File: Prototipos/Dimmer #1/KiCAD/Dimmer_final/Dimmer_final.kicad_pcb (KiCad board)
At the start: 2 copper layers, 50 x 100 mm, 32 parts, among them J2 Conn_01x02, K1 SRD-05VDC-SL-C, M5_BotL MountingHole_5.3mm_M5, M5_BotR MountingHole_5.3mm_M5, M5_TopL MountingHole_5.3mm_M5, M5_TopR MountingHole_5.3mm_M5, Q1 BC548B, Q2 BT137, U1 MOC3021M, U2 EL817

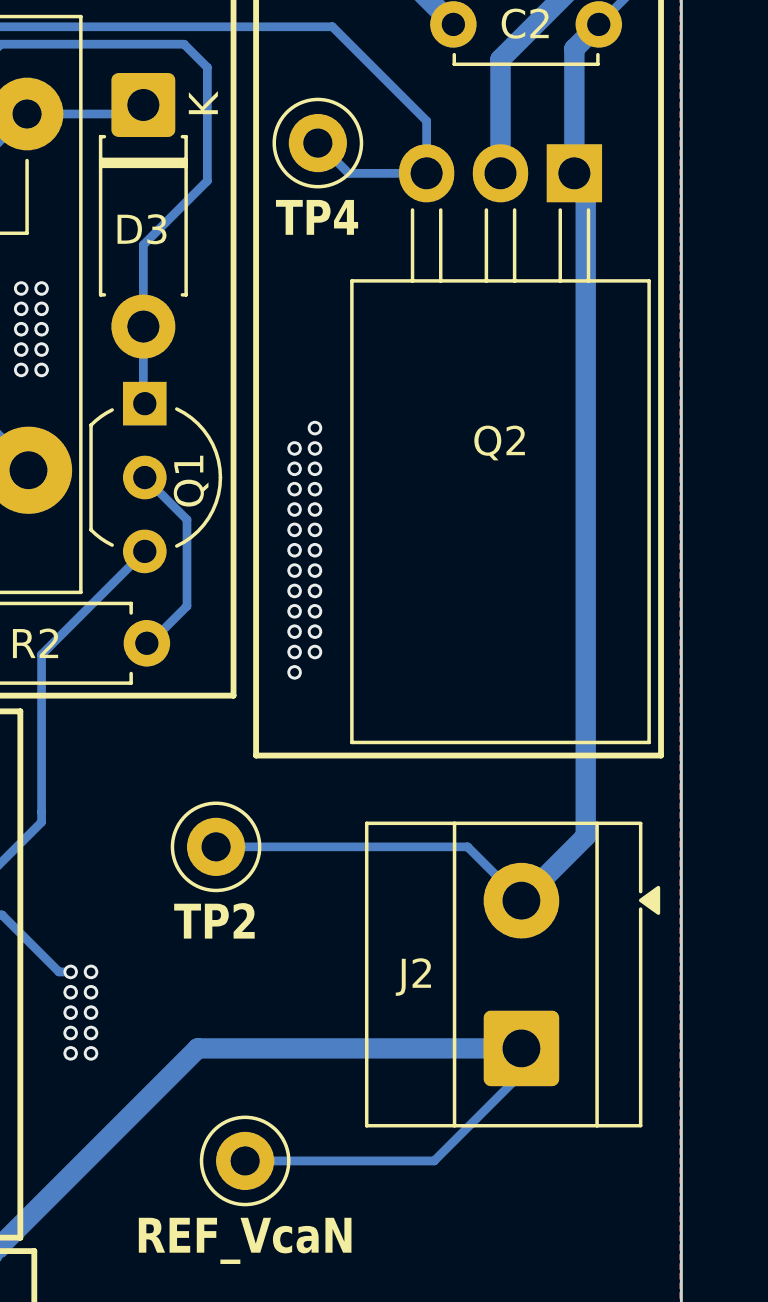
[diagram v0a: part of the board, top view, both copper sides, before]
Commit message: Actualizar footprints
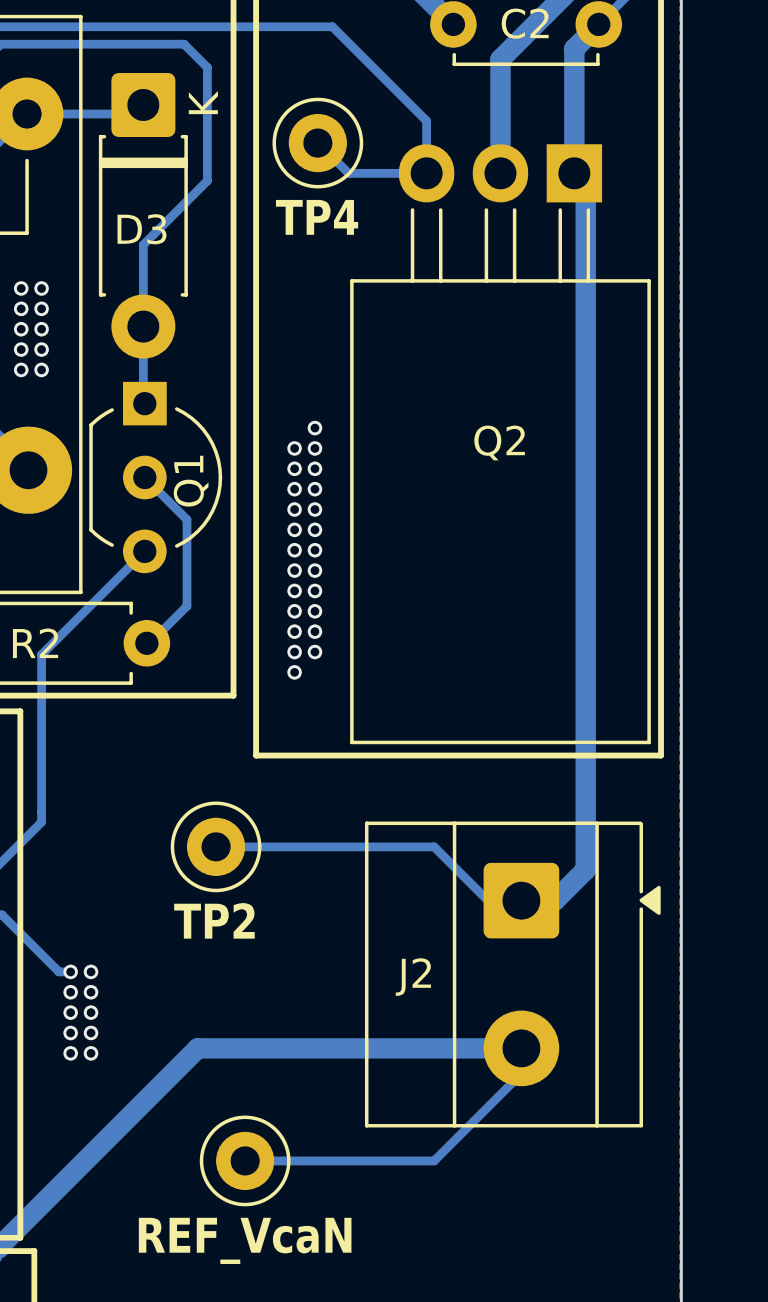
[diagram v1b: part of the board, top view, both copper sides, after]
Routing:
- net LOAD_L: track 87.8 -> 88.4 mm
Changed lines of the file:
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@@
 		)
 		(embedded_fonts no)
-		(model "${KIPRJMOD}/../../../../KiCad-Libraries/RV09AF-40-20K-B10K--3DModel-STEP-510211.STEP"
+		(model "${KICAD9_3DMODEL_DIR}/Potentiometer_THT.3dshapes/Potentiometer_Alps_RK09K_Single_Vertical.step"
 			(offset
-				(xyz 7 -2.5 0)
+				(xyz 0 0 0)
 			)
 			(scale
@@
 			)
 			(rotate
-				(xyz -90 -0 90)
+				(xyz 0 0 0)
 			)
 		)
@@
 		)
 		(embedded_fonts no)
-		(model "${KIPRJMOD}/../../../../KiCad-Libraries/MOC3021.step"
-			(offset
-				(xyz 0 0 0)
-			)
-			(scale
-				(xyz 1 0.8 1.05)
-			)
-			(rotate
-				(xyz -90 -0 -0)
-			)
-		)
 	)
 	(footprint "TestPoint:TestPoint_Loop_D1.80mm_Drill1.0mm_Beaded"
@@
 		)
 		(fp_line
-			(start 5.39 4.1)
-			(end 7.726447 4.1)
+			(start 5.39 4.12)
+			(end 7.7 4.12)
 			(stroke
 				(width 0.12)
@@
 		)
 		(fp_line
-			(start -2.65 4.1)
-			(end 4.79 4.1)
+			(start -2.65 4.12)
+			(end 4.79 4.12)
 			(stroke
 				(width 0.12)
@@
 		)
 		(fp_line
-			(start -2.66 4.1)
+			(start -2.66 4.12)
 			(end -2.66 -5.32)
 			(stroke
@@
 		(fp_poly
 			(pts
-				(xy 5.09 4.1) (xy 4.65 4.71) (xy 5.53 4.71)
+				(xy 5.09 4.12) (xy 4.65 4.73) (xy 5.53 4.73)
 			)
 			(stroke
@@
 		(fp_line
 			(start 7.62 -5.2)
-			(end 7.62 4.6)
+			(end 7.62 4.1)
 			(stroke
 				(width 0.1)
@@
 		)
 		(fp_line
-			(start -2.54 4.1)
-			(end -2.54 -5.2)
+			(start 7.13 4)
+			(end 7.63 3.5)
 			(stroke
 				(width 0.1)
@@
 		)
 		(fp_line
-			(start -2.54 4.1)
-			(end 7.62 4.1)
+			(start -2.53 4)
+			(end 7.13 4)
 			(stroke
 				(width 0.1)
@@
 		)
 		(fp_line
-			(start 7.62 4.6)
-			(end -2.04 4.6)
+			(start -2.54 4.1)
+			(end -2.54 -5.2)
 			(stroke
 				(width 0.1)
@@
 		)
 		(fp_line
-			(start -2.04 4.6)
-			(end -2.54 4.1)
+			(start -2.54 4.1)
+			(end 7.62 4.1)
 			(stroke
 				(width 0.1)
@@
 			)
 		)
-		(pad "1" thru_hole roundrect
+		(pad "1" thru_hole circle
 			(at 0 0 90)
 			(size 2.6 2.6)
@@
 			(layers "*.Cu" "*.Mask")
 			(remove_unused_layers no)
-			(roundrect_rratio 0.096154)
 			(net 5 "48Vca_N")
 			(pinfunction "Pin_1")
 			(pintype "passive")
 		)
-		(pad "2" thru_hole circle
+		(pad "2" thru_hole roundrect
 			(at 5.08 0 90)
 			(size 2.6 2.6)
@@
 			(layers "*.Cu" "*.Mask")
 			(remove_unused_layers no)
+			(roundrect_rratio 0.09615384615)
 			(net 2 "LOAD_L")
 			(pinfunction "Pin_2")
@@
 		(tags "PCIe")
 		(property "Reference" "J4"
-			(at 11.32 -6.52 180)
+			(at 11.32 -6.52 0)
 			(layer "F.SilkS")
 			(effects
@@
 		)
 		(fp_text user "${REFERENCE}"
-			(at 11.52 -6.53 180)
+			(at 11.52 -6.53 0)
 			(layer "F.Fab")
 			(effects
@@
 	)
 	(segment
-		(start 110.32 57.45)
-		(end 109.69 57.45)
-		(width 0.3)
+		(start 137.65 102.55)
+		(end 138.71 101.49)
+		(width 0.7)
 		(layer "B.Cu")
 		(net 2)
 	)
 	(segment
-		(start 136.5 102.55)
-		(end 134.65 100.7)
+		(start 110.32 57.45)
+		(end 109.69 57.45)
 		(width 0.3)
 		(layer "B.Cu")
@@
 	)
 	(segment
-		(start 138.71 100.34)
+		(start 135.35 102.55)
+		(end 133.5 100.7)
+		(width 0.3)
+		(layer "B.Cu")
+		(net 2)
+	)
+	(segment
+		(start 136.5 102.55)
+		(end 135.35 102.55)
+		(width 0.3)
+		(layer "B.Cu")
+		(net 2)
+	)
+	(segment
+		(start 138.71 101.49)
 		(end 138.71 77.93)
 		(width 0.7)
@@
 	(segment
 		(start 136.5 102.55)
-		(end 138.71 100.34)
+		(end 137.65 102.55)
 		(width 0.7)
 		(layer "B.Cu")
@@
 	)
 	(segment
-		(start 134.65 100.7)
+		(start 133.5 100.7)
 		(end 126 100.7)
 		(width 0.3)

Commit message: Correcciones varias
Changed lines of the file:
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@@
 	)
 	(via
-		(at 114.9 50)
+		(at 114.9 47.9)
 		(size 0.5)
 		(drill 0.3)
@@
 	)
 	(via
-		(at 117 49.3)
+		(at 117 47.2)
 		(size 0.5)
 		(drill 0.3)
@@
 	)
 	(via
-		(at 119.8 49.3)
+		(at 119.8 47.2)
 		(size 0.5)
 		(drill 0.3)
@@
 	)
 	(via
-		(at 120.5 50)
+		(at 120.5 47.9)
 		(size 0.5)
 		(drill 0.3)
@@
 	)
 	(via
-		(at 116.3 50)
+		(at 116.3 47.9)
 		(size 0.5)
 		(drill 0.3)
@@
 	)
 	(via
-		(at 121.2 50)
-		(size 0.5)
-		(drill 0.3)
-		(layers "F.Cu" "B.Cu")
-		(net 11)
-	)
-	(via
-		(at 119.1 49.3)
+		(at 121.2 47.9)
+		(size 0.5)
+		(drill 0.3)
+		(layers "F.Cu" "B.Cu")
+		(net 11)
+	)
+	(via
+		(at 119.1 47.2)
 		(size 0.5)
 		(drill 0.3)
@@
 	)
 	(via
-		(at 113.5 50)
+		(at 113.5 47.9)
 		(size 0.5)
 		(drill 0.3)
@@
 	)
 	(via
-		(at 112.8 49.3)
+		(at 112.8 47.2)
 		(size 0.5)
 		(drill 0.3)
@@
 	)
 	(via
-		(at 120.5 49.3)
+		(at 120.5 47.2)
 		(size 0.5)
 		(drill 0.3)
@@
 	)
 	(via
-		(at 115.6 49.3)
-		(size 0.5)
-		(drill 0.3)
-		(layers "F.Cu" "B.Cu")
-		(net 11)
-	)
-	(via
-		(at 117 50)
+		(at 115.6 47.2)
+		(size 0.5)
+		(drill 0.3)
+		(layers "F.Cu" "B.Cu")
+		(net 11)
+	)
+	(via
+		(at 117 47.9)
 		(size 0.5)
 		(drill 0.3)
@@
 	)
 	(via
-		(at 117.7 49.3)
-		(size 0.5)
-		(drill 0.3)
-		(layers "F.Cu" "B.Cu")
-		(net 11)
-	)
-	(via
-		(at 114.2 50)
+		(at 117.7 47.2)
+		(size 0.5)
+		(drill 0.3)
+		(layers "F.Cu" "B.Cu")
+		(net 11)
+	)
+	(via
+		(at 114.2 47.9)
 		(size 0.5)
 		(drill 0.3)
@@
 	)
 	(via
-		(at 114.2 49.3)
+		(at 114.2 47.2)
 		(size 0.5)
 		(drill 0.3)
@@
 	)
 	(via
-		(at 118.4 49.3)
+		(at 118.4 47.2)
 		(size 0.5)
 		(drill 0.3)
@@
 	)
 	(via
-		(at 115.6 50)
+		(at 115.6 47.9)
 		(size 0.5)
 		(drill 0.3)
@@
 	)
 	(via
-		(at 113.5 49.3)
+		(at 113.5 47.2)
 		(size 0.5)
 		(drill 0.3)
@@
 	)
 	(via
-		(at 117.7 50)
+		(at 117.7 47.9)
 		(size 0.5)
 		(drill 0.3)
@@
 	)
 	(via
-		(at 114.9 49.3)
+		(at 114.9 47.2)
 		(size 0.5)
 		(drill 0.3)
@@
 	)
 	(via
-		(at 119.8 50)
+		(at 119.8 47.9)
 		(size 0.5)
 		(drill 0.3)
@@
 	)
 	(via
-		(at 118.4 50)
+		(at 118.4 47.9)
 		(size 0.5)
 		(drill 0.3)
@@
 	)
 	(via
-		(at 119.1 50)
+		(at 119.1 47.9)
 		(size 0.5)
 		(drill 0.3)
@@
 	)
 	(via
-		(at 116.3 49.3)
-		(size 0.5)
-		(drill 0.3)
+		(at 116.3 47.2)
+		(size 0.5)
+		(drill 0.3)

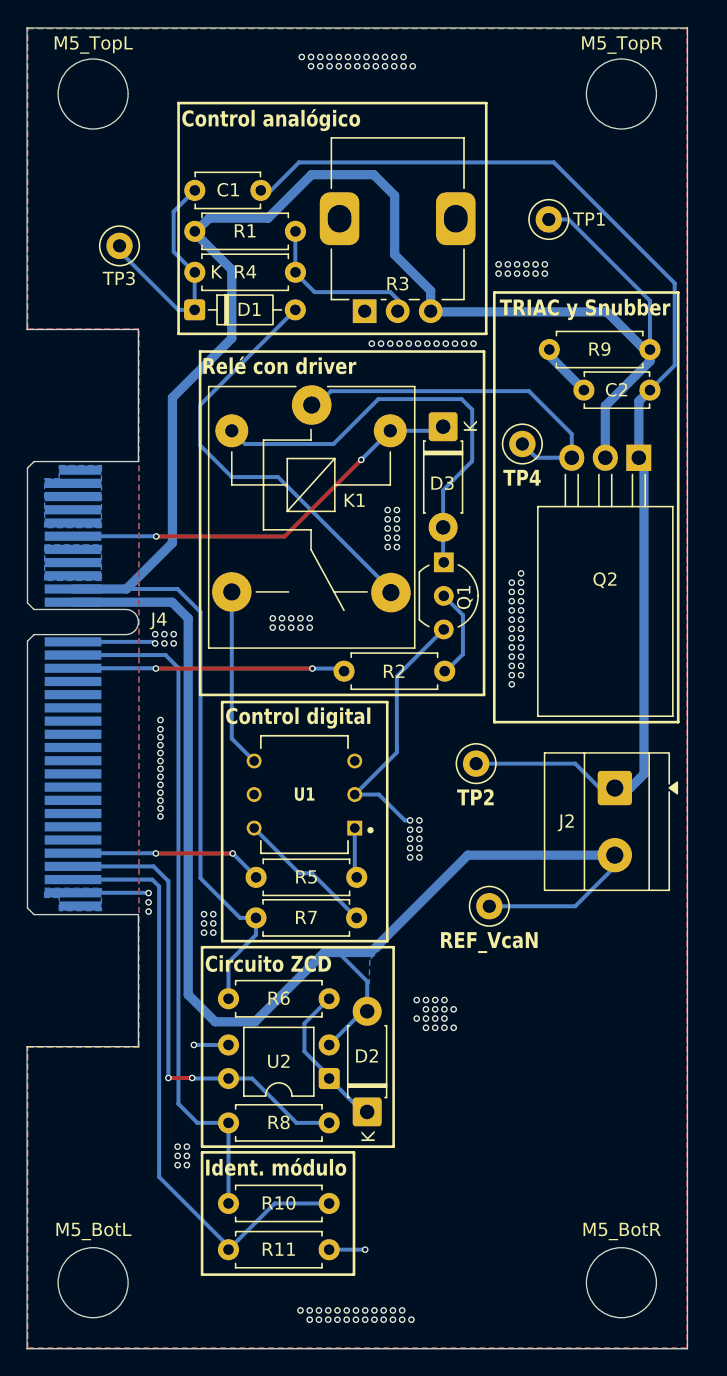
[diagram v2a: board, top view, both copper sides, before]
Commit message: Agregar titulo de módulo y firma
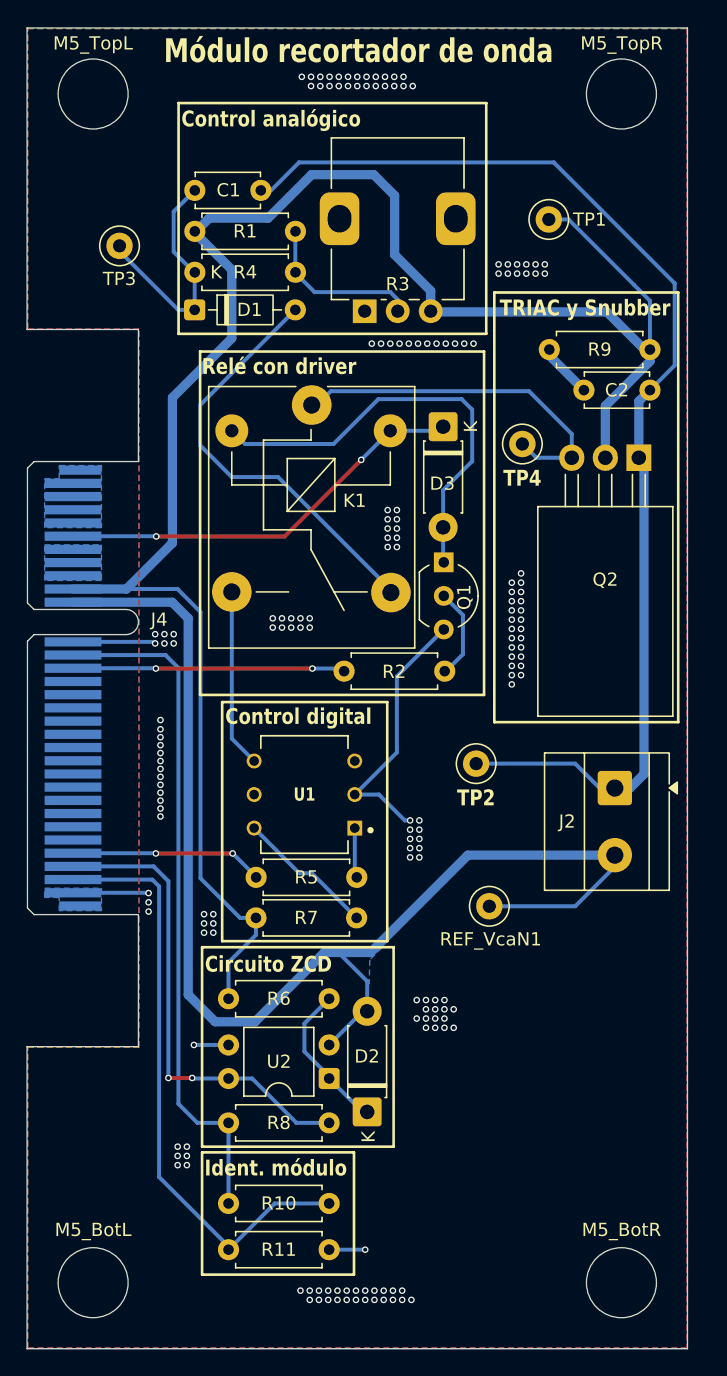
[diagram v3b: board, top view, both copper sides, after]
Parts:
- removed REF_VcaN: TestPoint_Loop_D1.80mm_Drill1.0mm_Beaded, TestPoint:TestPoint_Loop_D1.80mm_Drill1.0mm_Beaded
- added REF_VcaN1: TestPoint, TestPoint:TestPoint_Loop_D1.80mm_Drill1.0mm_Beaded, F.Cu at (127.0, 111.5)
- D2, D3: value D_Small -> 1N4007
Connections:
- net UC_DOUT renamed uC_DOUT
- net UC_PHASE renamed uC_PHASE
- net UC_RELAY renamed uC_RELAY
- R3 pad MP: AGND -> (no net)
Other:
- board text added: "Módulo recortador de onda"
- board text added: "NSH Designs"

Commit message: Agregar firma con nombres
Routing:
- net LOAD_L: track 88.4 -> 87.3 mm
- net AGND: vias 178 -> 177
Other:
- board text added: "Alesandria, A. S. Cignetti, M. A. Galliano, I."
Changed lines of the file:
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@@
 		(tags "test point wire loop bead")
 		(property "Reference" "TP3"
-			(at 0 2.5 0)
+			(at 0 2.6 0)
 			(layer "F.SilkS")
 			(effects
 				(font
-					(size 1 1)
-					(thickness 0.15)
+					(size 1.2 1)
+					(thickness 0.2)
+					(bold yes)
 				)
 			)
@@
 		(tags "Diode DO-35_SOD27 series Axial Horizontal pin pitch 7.62mm  length 4mm diameter 2mm")
 		(property "Reference" "D1"
-			(at 4.160064 0 0)
+			(at 4.710064 0 0)
 			(layer "F.SilkS")
 			(effects
@@
 		)
 		(fp_text user "K"
-			(at 1.624796 -2.845269 0)
+			(at 3.210064 0 0)
 			(layer "F.SilkS")
 			(effects
@@
 			(effects
 				(font
-					(size 1 1)
-					(thickness 0.15)
+					(size 1.2 1)
+					(thickness 0.2)
+					(bold yes)
 				)
 			)
@@
 	)
 	(gr_line
+		(start 139 120.3)
+		(end 139 134)
+		(stroke
+			(width 0.15)
+			(type solid)
+		)
+		(layer "B.SilkS")
+	)
+	(gr_line
 		(start 100.43 112.13)
 		(end 100.43 122.13)
@@
 		)
 	)
+	(gr_text "Alesandria, A. S. \nCignetti, M. A.\nGalliano, I."
+		(at 138.4 120.1 90)
+		(layer "B.SilkS")
+		(effects
+			(font
+				(size 0.9 1)
+				(thickness 0.15)
+			)
+			(justify left bottom mirror)
+		)
+	)
 	(gr_text "NSH Designs"
 		(at 141.3 120.2 90)
@@
 	)
 	(segment
-		(start 137.65 102.55)
-		(end 138.71 101.49)
-		(width 0.7)
+		(start 131.88 55.18)
+		(end 112.59 55.18)
+		(width 0.3)
 		(layer "B.Cu")
 		(net 2)
 	)
 	(segment
-		(start 110.32 57.45)
-		(end 109.69 57.45)
+		(start 139.16 72.42)
+		(end 140.9 70.68)
 		(width 0.3)
 		(layer "B.Cu")
@@
 	)
 	(segment
-		(start 138.71 77.93)
-		(end 138.32 77.54)
-		(width 0.7)
+		(start 110.32 57.45)
+		(end 109.69 57.45)
+		(width 0.3)
 		(layer "B.Cu")
 		(net 2)
@@
 	)
 	(segment
-		(start 136.5 102.55)
-		(end 135.35 102.55)
-		(width 0.3)
+		(start 138.32 79.98)
+		(end 136.5 81.8)
+		(width 0.7)
 		(layer "B.Cu")
 		(net 2)
 	)
 	(segment
-		(start 138.71 101.49)
-		(end 138.71 77.93)
-		(width 0.7)
+		(start 136.5 102.55)
+		(end 135.35 102.55)
+		(width 0.3)
 		(layer "B.Cu")
 		(net 2)
@@
 	)
 	(segment
-		(start 141.03 70.55)
-		(end 141.03 64.33)
+		(start 140.9 64.2)
+		(end 131.88 55.18)
 		(width 0.3)
 		(layer "B.Cu")
@@
 	)
 	(segment
-		(start 136.5 102.55)
-		(end 137.65 102.55)
-		(width 0.7)
+		(start 112.59 55.18)
+		(end 110.32 57.45)
+		(width 0.3)
 		(layer "B.Cu")
 		(net 2)
 	)
 	(segment
-		(start 141.03 64.33)
-		(end 131.88 55.18)
-		(width 0.3)
+		(start 138.32 77.54)
+		(end 138.32 79.98)
+		(width 0.7)
 		(layer "B.Cu")
 		(net 2)
 	)
 	(segment
-		(start 139.16 72.42)
-		(end 141.03 70.55)
-		(width 0.3)
+		(start 136.5 81.8)
+		(end 136.5 102.55)
+		(width 0.7)
 		(layer "B.Cu")
 		(net 2)
@@
 	)
 	(segment
-		(start 112.59 55.18)
-		(end 110.32 57.45)
-		(width 0.3)
-		(layer "B.Cu")
-		(net 2)
-	)
-	(segment
-		(start 131.88 55.18)
-		(end 112.59 55.18)
+		(start 140.9 70.68)
+		(end 140.9 64.2)
 		(width 0.3)
 		(layer "B.Cu")
@@
 	)
 	(via
-		(at 102.1 101.7)
+		(at 102.1 102.3)
 		(size 0.5)
 		(drill 0.3)
@@
 	)
 	(via
-		(at 102.1 104.1)
+		(at 102.1 104.4)
 		(size 0.5)
 		(drill 0.3)
@@
 	)
 	(via
-		(at 102.1 99.9)
+		(at 102.1 100.2)
 		(size 0.5)
 		(drill 0.3)
@@
 	)
 	(via
-		(at 102.1 102.9)
+		(at 102.1 103)
 		(size 0.5)
 		(drill 0.3)
@@
 	)
 	(via
-		(at 102.1 100.5)
+		(at 102.1 100.9)
 		(size 0.5)
 		(drill 0.3)
@@
 	)
 	(via
-		(at 102.1 98.7)
+		(at 102.1 98.8)
 		(size 0.5)
 		(drill 0.3)
@@
 	)
 	(via
-		(at 102.1 104.7)
+		(at 102.1 105.1)
 		(size 0.5)
 		(drill 0.3)
@@
 	)
 	(via
-		(at 102.1 102.3)
-		(size 0.5)
-		(drill 0.3)
-		(layers "F.Cu" "B.Cu")
-		(net 11)
-	)
-	(via
 		(at 123.6 120.7)
 		(size 0.5)
@@
 	)
 	(via
-		(at 102.1 101.1)
+		(at 102.1 101.6)
 		(size 0.5)
 		(drill 0.3)
@@
 	)
 	(via
-		(at 102.1 99.3)
+		(at 102.1 99.5)
 		(size 0.5)
 		(drill 0.3)
@@
 	)
 	(via
-		(at 102.1 103.5)
+		(at 102.1 103.7)
 		(size 0.5)
 		(drill 0.3)
@@
 	)
 	(segment
-		(start 135.78 73.62)
-		(end 139.16 70.24)
+		(start 135.78 74.92)
+		(end 136.5 74.2)
 		(width 0.7)
 		(layer "B.Cu")
@@
 	)
 	(segment
+		(start 136.5 74.2)
+		(end 136.5 72.01)
+		(width 0.7)
+		(layer "B.Cu")
+		(net 13)
+	)
+	(segment
 		(start 105.79 59.4)
 		(end 104.79 60.4)
@@
 	(segment
 		(start 135.78 77.54)
-		(end 135.78 73.62)
+		(end 135.78 74.92)
 		(width 0.7)
 		(layer "B.Cu")
@@
 	)
 	(segment
-		(start 139.16 70.24)
-		(end 139.16 69.35)
-		(width 0.7)
-		(layer "B.Cu")
-		(net 13)
-	)
-	(segment
 		(start 107.5 63.31)
 		(end 107.5 68.5)
@@
 	)
 	(segment
+		(start 136.5 72.01)
+		(end 139.16 69.35)
+		(width 0.7)
+		(layer "B.Cu")
+		(net 13)
+	)
+	(segment
 		(start 139.16 69.35)
 		(end 138.75 69.35)
@@
 		(polygon
 			(pts
-				(xy 118.85 114.65) (xy 117.95 115.55) (xy 117.9 117.4) (xy 115.75 115.15)
+				(xy 118.85 114.65) (xy 117.9 115.6) (xy 117.9 117.4) (xy 115.75 115.15)
 			)
 		)
@@
 			"5fdd23a6-cfe0-4abc-a5ac-c833b26c1df6" "668f50ad-9608-4b6c-92fa-4e1b13ae1f87"
 			"6a968e24-07f5-4c34-8d29-74e528ee73cb" "77b93d64-23f2-46bf-bb5e-87463bd74535"
-			"8ace8079-af4d-4b2e-ac81-9cdc9338dd86" "8bc37bd8-da70-4ed2-b598-9c8f7934e0ff"
-			"a4607091-be90-4484-b8c0-d32f0e672aba" "f0b0d27a-4ff7-4a1a-b55c-448616dfeebe"
-			"fd3b0bd8-1bb7-4fbf-97e5-eae7270816f2"
+			"8bc37bd8-da70-4ed2-b598-9c8f7934e0ff" "a4607091-be90-4484-b8c0-d32f0e672aba"
+			"f0b0d27a-4ff7-4a1a-b55c-448616dfeebe" "fd3b0bd8-1bb7-4fbf-97e5-eae7270816f2"
 		)
 	)
@@
 		)
 	)
+	(group ""
+		(members "207fdee4-6f41-46fb-8464-1b34683ee91a" "858e8ef2-552e-4327-8b94-83602f54523e"
+			"964e7497-cf91-41c6-ba2b-ba55fb42b453"
+		)
+	)
